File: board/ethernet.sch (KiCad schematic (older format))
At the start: 61 parts, among them IC5 KSZ8081RNx, IC6 MAX5969x, IC7 MAX17503, J1 RJHSE-538B, T1 749010012A, Y2 25MHz

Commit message: Final finishing touches and gerbers
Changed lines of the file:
@@
 	1    0    0    -1
 $EndComp
-Text Label 5150 4300 0    60   ~ 0
-+48V
 Wire Wire Line
 	1200 1950 1500 1950
@@
 $Comp
 L PWR_FLAG #FLG072
-U 0 1 58E0F72D
+U 1 1 58E0F72D
 P 10100 4850
 F 0 "#FLG072" H 10100 4925 50  0001 C CNN
@@
 F 2 "" H 10100 4850 50  0001 C CNN
 F 3 "" H 10100 4850 50  0001 C CNN
-	0    10100 4850
+	1    10100 4850
 	1    0    0    -1
 $EndComp
@@
 $Comp
 L PWR_FLAG #FLG073
-U 0 1 58E11EB9
+U 1 1 58E11EB9
 P 3100 4550
 F 0 "#FLG073" H 3100 4625 50  0001 C CNN
@@
 F 2 "" H 3100 4550 50  0001 C CNN
 F 3 "" H 3100 4550 50  0001 C CNN
-	0    3100 4550
+	1    3100 4550
 	1    0    0    -1
 $EndComp
@@
 $Comp
 L PWR_FLAG #FLG074
-U 0 1 58E13788
+U 1 1 58E13788
 P 3100 5500
 F 0 "#FLG074" H 3100 5575 50  0001 C CNN
@@
 F 2 "" H 3100 5500 50  0001 C CNN
 F 3 "" H 3100 5500 50  0001 C CNN
-	0    3100 5500
+	1    3100 5500
 	-1   0    0    1
 $EndComp
@@
 $Comp
 L PWR_FLAG #FLG075
-U 0 1 58E16BA0
+U 1 1 58E16BA0
 P 6150 4200
 F 0 "#FLG075" H 6150 4275 50  0001 C CNN
@@
 F 2 "" H 6150 4200 50  0001 C CNN
 F 3 "" H 6150 4200 50  0001 C CNN
-	0    6150 4200
+	1    6150 4200
 	1    0    0    -1
 $EndComp
@@
 $Comp
 L PWR_FLAG #FLG076
-U 0 1 58E174E3
+U 1 1 58E174E3
 P 6600 800
 F 0 "#FLG076" H 6600 875 50  0001 C CNN
@@
 F 2 "" H 6600 800 50  0001 C CNN
 F 3 "" H 6600 800 50  0001 C CNN
-	0    6600 800
+	1    6600 800
 	1    0    0    -1
 $EndComp
@@
 Wire Wire Line
 	1450 2550 1450 2400
+$Comp
+L +48V #PWR077
+U 1 1 58DEF5C6
+P 5200 4150
+F 0 "#PWR077" H 5200 4000 50  0001 C CNN
+F 1 "+48V" V 5215 4278 50  0000 L CNN
+F 2 "" H 5200 4150 50  0001 C CNN
+F 3 "" H 5200 4150 50  0001 C CNN
+	1    5200 4150
+	0    1    1    0
+$EndComp
+Wire Wire Line
+	5200 4150 5200 4300
+Connection ~ 5200 4300
 $EndSCHEMATC

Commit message: Order codes for capacitor shrapnel
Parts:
- C24, C26, C28, C33, C34, C39: Farnell (none) -> 2522597
- C27: Farnell (none) -> 1735526
- C35: Farnell (none) -> 2494230
- C36, C37: Farnell (none) -> 2524889
- C42: Farnell (none) -> 2522598
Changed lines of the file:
@@
 F 2 "agg:0603" H 5288 2850 50  0001 C CNN
 F 3 "" H 5250 3000 50  0000 C CNN
+F 4 "2522597" H 5250 3000 60  0001 C CNN "Farnell"
 	1    5250 3000
 	1    0    0    -1
@@
 F 2 "agg:0603" H 6938 3200 50  0001 C CNN
 F 3 "" H 6900 3350 50  0000 C CNN
+F 4 "2524889" H 6900 3350 60  0001 C CNN "Farnell"
 	1    6900 3350
 	1    0    0    -1
@@
 F 2 "agg:0603" H 6538 1850 50  0001 C CNN
 F 3 "" H 6500 2000 50  0000 C CNN
+F 4 "1735526" H 6500 2000 60  0001 C CNN "Farnell"
 	1    6500 2000
 	1    0    0    -1
@@
 F 2 "agg:0603" H 6988 1850 50  0001 C CNN
 F 3 "" H 6950 2000 50  0000 C CNN
+F 4 "2522597" H 6950 2000 60  0001 C CNN "Farnell"
 	1    6950 2000
 	1    0    0    -1
@@
 F 2 "agg:0603" H 10238 3050 50  0001 C CNN
 F 3 "" H 10200 3200 50  0000 C CNN
+F 4 "2494230" H 10200 3200 60  0001 C CNN "Farnell"
 	1    10200 3200
 	1    0    0    -1
@@
 F 2 "agg:0603" H 5688 2850 50  0001 C CNN
 F 3 "" H 5650 3000 50  0000 C CNN
+F 4 "2522597" H 5650 3000 60  0001 C CNN "Farnell"
 	1    5650 3000
 	1    0    0    -1
@@
 F 2 "agg:0603" H 7338 3200 50  0001 C CNN
 F 3 "" H 7300 3350 50  0000 C CNN
+F 4 "2524889" H 7300 3350 60  0001 C CNN "Farnell"
 	1    7300 3350
 	1    0    0    -1
@@
 F 2 "agg:0603" H 6888 1400 50  0001 C CNN
 F 3 "" H 6850 1550 50  0000 C CNN
+F 4 "2522597" H 6850 1550 60  0001 C CNN "Farnell"
 	1    6850 1550
 	1    0    0    -1
@@
 F 2 "agg:0603" H 6888 850 50  0001 C CNN
 F 3 "" H 6850 1000 50  0000 C CNN
+F 4 "2522597" H 6850 1000 60  0001 C CNN "Farnell"
 	1    6850 1000
 	1    0    0    -1
@@
 F 2 "agg:0603" H 6238 5400 50  0001 C CNN
 F 3 "" H 6200 5550 50  0000 C CNN
+F 4 "2522598" H 6200 5550 60  0001 C CNN "Farnell"
 	1    6200 5550
 	1    0    0    -1
@@
 F 2 "agg:0603" H 8088 4500 50  0001 C CNN
 F 3 "" H 8050 4650 50  0000 C CNN
+F 4 "2522597" H 8050 4650 60  0001 C CNN "Farnell"
 	1    8050 4650
 	1    0    0    -1

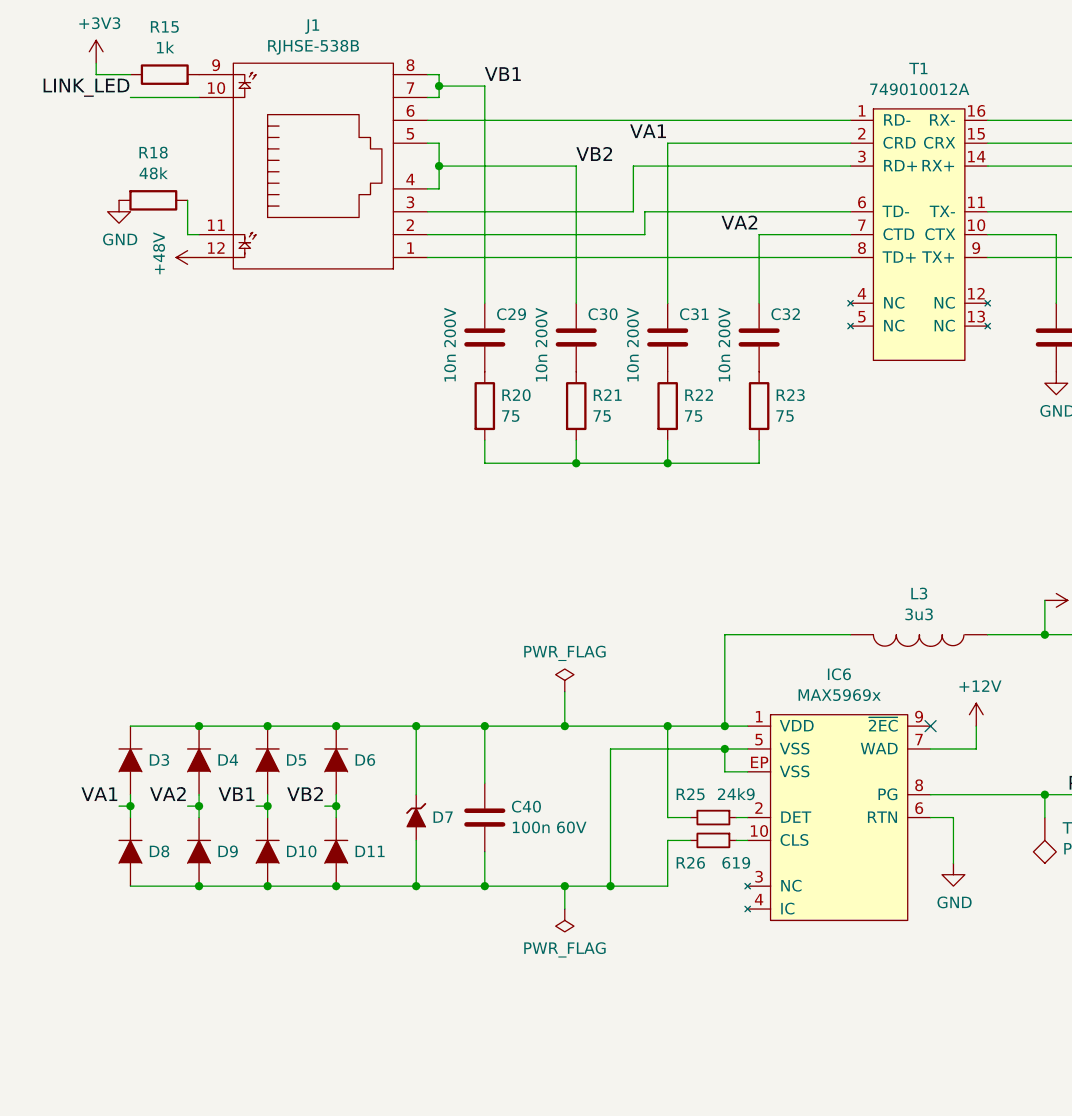
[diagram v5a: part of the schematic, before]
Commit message: specced remaining parts
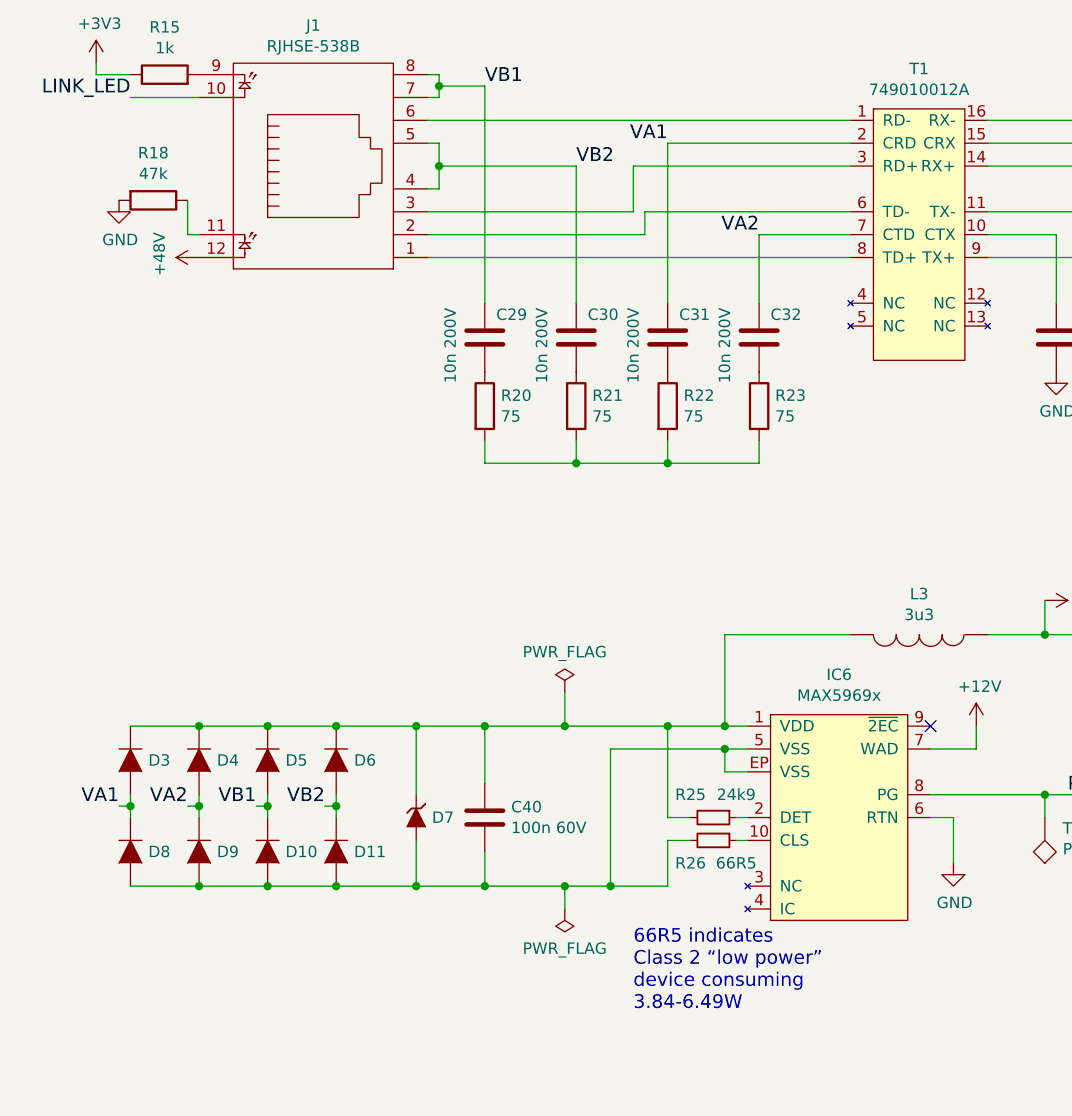
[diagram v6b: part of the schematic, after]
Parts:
- D10, D11, D3, D4, D5, D6, D8, D9: Farnell (none) -> 1861422
- D2: Farnell (none) -> 1466524
- D7: Farnell (none) -> 1899460
- L2: Farnell (none) -> 1463451
- R11, R12, R13, R14: Farnell (none) -> 9238301
- R15, R16: Farnell (none) -> 9238484
- R17: Farnell (none) -> 2141552
- R18: value 48k -> 47k; Farnell (none) -> 9233580
- R19: Farnell (none) -> 9238603
- R20, R21, R22, R23: Farnell (none) -> 2059571
- R25: Farnell (none) -> 1469785
- R26: value 619 -> 66R5; Farnell (none) -> 2670874
- Y2: Farnell (none) -> 2101328
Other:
- note added: "66R5 indicates\nClass 2 “low power”\ndevice consuming\n3.84-6.49W"
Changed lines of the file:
@@
 F 2 "agg:0603" V 2680 3300 50  0001 C CNN
 F 3 "" H 2750 3300 50  0000 C CNN
+F 4 "2059571" H 2750 3300 60  0001 C CNN "Farnell"
 	1    2750 3300
 	1    0    0    -1
@@
 F 1 "25MHz" V 6555 2769 50  0000 R CNN
 F 2 "agg:XTAL-50x32" H 6600 2900 50  0001 C CNN
-F 3 "" H 6600 2900 50  0000 C CNN
+F 3 "http://www.farnell.com/datasheets/1754353.pdf" H 6600 2900 50  0001 C CNN
+F 4 "2101328" H 6600 2900 60  0001 C CNN "Farnell"
 	1    6600 2900
 	0    -1   -1   0
@@
 F 1 "FB" V 6163 850 50  0000 C CNN
 F 2 "agg:0603" H 6250 850 50  0001 C CNN
-F 3 "" H 6250 850 50  0000 C CNN
+F 3 "http://www.farnell.com/datasheets/2005683.pdf" H 6250 850 50  0001 C CNN
+F 4 "1463451" H 6250 850 60  0001 C CNN "Farnell"
 	1    6250 850
 	0    1    1    0
@@
 F 2 "agg:0603" H 8800 1550 50  0001 C CNN
 F 3 "" H 8800 1550 50  0000 C CNN
+F 4 "9238301" H 8800 1550 60  0001 C CNN "Farnell"
 	1    8800 1550
 	0    1    1    0
@@
 F 2 "agg:0603" H 9550 2250 50  0001 C CNN
 F 3 "" H 9550 2250 50  0000 C CNN
+F 4 "9238484" H 9550 2250 60  0001 C CNN "Farnell"
 	1    9550 2250
 	1    0    0    -1
@@
 F 2 "agg:0603" V 9480 2750 50  0001 C CNN
 F 3 "" H 9550 2750 50  0000 C CNN
+F 4 "2141552" H 9550 2750 60  0001 C CNN "Farnell"
 	1    9550 2750
 	0    -1   -1   0
@@
 F 1 "1N4148" V 9995 2978 50  0000 L CNN
 F 2 "agg:SOD-323" H 9950 2900 50  0001 C CNN
-F 3 "" H 9950 2900 50  0000 C CNN
+F 3 "http://www.farnell.com/datasheets/1695880.pdf" H 9950 2900 50  0001 C CNN
+F 4 "1466524" H 9950 2900 60  0001 C CNN "Farnell"
 	1    9950 2900
 	0    1    1    0
@@
 F 2 "agg:0603" V 10380 2900 50  0001 C CNN
 F 3 "" H 10450 2900 50  0000 C CNN
+F 4 "9238603" H 10450 2900 60  0001 C CNN "Farnell"
 	1    10450 2900
 	1    0    0    -1
@@
 F 2 "agg:0603" V 1280 1850 50  0001 C CNN
 F 3 "" H 1350 1850 50  0000 C CNN
+F 4 "9238484" H 1350 1850 60  0001 C CNN "Farnell"
 	1    1350 1850
 	0    -1   -1   0
@@
 F 2 "agg:0603" V 3080 3300 50  0001 C CNN
 F 3 "" H 3150 3300 50  0000 C CNN
+F 4 "2059571" H 3150 3300 60  0001 C CNN "Farnell"
 	1    3150 3300
 	1    0    0    -1
@@
 F 2 "agg:0603" V 3480 3300 50  0001 C CNN
 F 3 "" H 3550 3300 50  0000 C CNN
+F 4 "2059571" H 3550 3300 60  0001 C CNN "Farnell"
 	1    3550 3300
 	1    0    0    -1
@@
 F 2 "agg:0603" V 3880 3300 50  0001 C CNN
 F 3 "" H 3950 3300 50  0000 C CNN
+F 4 "2059571" H 3950 3300 60  0001 C CNN "Farnell"
 	1    3950 3300
 	1    0    0    -1
@@
 F 2 "agg:0603" H 8800 1650 50  0001 C CNN
 F 3 "" H 8800 1650 50  0000 C CNN
+F 4 "9238301" H 8800 1650 60  0001 C CNN "Farnell"
 	1    8800 1650
 	0    1    1    0
@@
 F 2 "agg:0603" H 8800 1750 50  0001 C CNN
 F 3 "" H 8800 1750 50  0000 C CNN
+F 4 "9238301" H 8800 1750 60  0001 C CNN "Farnell"
 	1    8800 1750
 	0    1    1    0
@@
 F 2 "agg:0603" H 8800 1850 50  0001 C CNN
 F 3 "" H 8800 1850 50  0000 C CNN
+F 4 "9238301" H 8800 1850 60  0001 C CNN "Farnell"
 	1    8800 1850
 	0    1    1    0
@@
 F 1 "SS110B" V 1245 4928 50  0001 L CNN
 F 2 "agg:DO-214AA-SMB" H 1200 4973 50  0001 C CNN
-F 3 "" H 1200 4850 50  0000 C CNN
+F 3 "http://www.farnell.com/datasheets/1441693.pdf" H 1200 4850 50  0001 C CNN
+F 4 "1861422" H 1200 4850 60  0001 C CNN "Farnell"
 	1    1200 4850
 	0    1    1    0
@@
 F 2 "agg:DO-214AA-SMB" H 1200 5373 50  0001 C CNN
 F 3 "" H 1200 5250 50  0000 C CNN
+F 4 "1861422" H 1200 5250 60  0001 C CNN "Farnell"
 	1    1200 5250
 	0    1    1    0
@@
 F 2 "agg:DO-214AA-SMB" H 1500 4973 50  0001 C CNN
 F 3 "" H 1500 4850 50  0000 C CNN
+F 4 "1861422" H 1500 4850 60  0001 C CNN "Farnell"
 	1    1500 4850
 	0    1    1    0
@@
 F 2 "agg:DO-214AA-SMB" H 1500 5373 50  0001 C CNN
 F 3 "" H 1500 5250 50  0000 C CNN
+F 4 "1861422" H 1500 5250 60  0001 C CNN "Farnell"
 	1    1500 5250
 	0    1    1    0
@@
 F 2 "agg:DO-214AA-SMB" H 1800 4973 50  0001 C CNN
 F 3 "" H 1800 4850 50  0000 C CNN
+F 4 "1861422" H 1800 4850 60  0001 C CNN "Farnell"
 	1    1800 4850
 	0    1    1    0
@@
 F 2 "agg:DO-214AA-SMB" H 1800 5373 50  0001 C CNN
 F 3 "" H 1800 5250 50  0000 C CNN
+F 4 "1861422" H 1800 5250 60  0001 C CNN "Farnell"
 	1    1800 5250
 	0    1    1    0
@@
 F 2 "agg:DO-214AA-SMB" H 2100 4973 50  0001 C CNN
 F 3 "" H 2100 4850 50  0000 C CNN
+F 4 "1861422" H 2100 4850 60  0001 C CNN "Farnell"
 	1    2100 4850
 	0    1    1    0
@@
 F 2 "agg:DO-214AA-SMB" H 2100 5373 50  0001 C CNN
 F 3 "" H 2100 5250 50  0000 C CNN
+F 4 "1861422" H 2100 5250 60  0001 C CNN "Farnell"
 	1    2100 5250
 	0    1    1    0
@@
 F 1 "SMAJ58A" H 2450 5215 50  0001 C CNN
 F 2 "agg:DO-214AC-SMA" H 2450 5100 50  0001 C CNN
-F 3 "" H 2450 5100 50  0000 C CNN
+F 3 "http://www.farnell.com/datasheets/2076055.pdf" H 2450 5100 50  0001 C CNN
+F 4 "1899460" H 2450 5100 60  0001 C CNN "Farnell"
 	1    2450 5100
 	0    1    1    0
@@
 F 2 "agg:0603" H 3750 5100 50  0001 C CNN
 F 3 "" H 3750 5100 50  0000 C CNN
+F 4 "1469785" H 3750 5100 60  0001 C CNN "Farnell"
 	1    3750 5100
 	0    1    1    0
@@
 P 3750 5200
 F 0 "R26" V 3850 5100 50  0000 C CNN
-F 1 "619" V 3850 5300 50  0000 C CNN
+F 1 "66R5" V 3850 5300 50  0000 C CNN
 F 2 "agg:0603" H 3750 5200 50  0001 C CNN
 F 3 "" H 3750 5200 50  0000 C CNN
+F 4 "2670874" H 3750 5200 60  0001 C CNN "Farnell"
 	1    3750 5200
 	0    1    1    0
@@
 Wire Wire Line
 	9950 2650 10450 2650
-Wire Wire Line
-	10450 2650 10450 2750
 Wire Wire Line
 	10200 2600 10200 2650
@@
 P 1300 2400
 F 0 "R18" V 1093 2400 50  0000 C CNN
-F 1 "48k" V 1184 2400 50  0000 C CNN
+F 1 "47k" V 1184 2400 50  0000 C CNN
 F 2 "agg:0603" V 1230 2400 50  0001 C CNN
 F 3 "" H 1300 2400 50  0001 C CNN
+F 4 "9233580" H 1300 2400 60  0001 C CNN "Farnell"
 	1    1300 2400
 	0    1    1    0
@@
 	5200 4150 5200 4300
 Connection ~ 5200 4300
+Wire Wire Line
+	10450 2650 10450 2750
+Text Notes 3400 5950 0    60   ~ 0
+66R5 indicates\nClass 2 “low power”\ndevice consuming\n3.84-6.49W
 $EndSCHEMATC
